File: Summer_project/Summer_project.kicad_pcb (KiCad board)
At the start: 2 copper layers, 15 parts, among them Q3 2N3904, Q4 2N3904, SW1 SW_Push

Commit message: rsc_3leds_battery
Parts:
- moved BT1 41.1 mm to (148.0, 124.0)
- moved C1 41.1 mm to (147.5, 55.0)
- moved C2 41.1 mm to (131.0, 80.5)
- moved D1 41.1 mm to (148.2, 72.0)
- moved D2 41.1 mm to (133.5, 57.0)
- moved D3 41.1 mm to (162.7, 57.0)
- moved Q3 41.1 mm to (126.5, 72.5)
- moved Q4 41.1 mm to (136.5, 72.5)
- moved R1 41.1 mm to (170.0, 93.3)
- moved R2 41.1 mm to (137.0, 85.7)
- moved R3 41.1 mm to (146.5, 85.7)
- moved R4 41.1 mm to (127.0, 85.7)
- moved R5 41.1 mm to (159.0, 85.7)
- moved SW1 41.1 mm to (151.2, 107.2)
- moved G*** 38.0 mm to (314.6, 141.0)
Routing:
- net Net-(D3-K): track 38.8 -> 40.7 mm

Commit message: _version_of_pcb_upgrades
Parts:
- moved G*** 167.0 mm to (149.0, 120.0)
- moved Q4 25.5 mm to (162.0, 72.5)
- moved C2 17.5 mm to (148.5, 79.5)
- moved C1 8.06 mm to (148.5, 63.0)
- moved Q3 7.46 mm to (134.0, 72.5)
- moved R4 6.50 mm to (133.5, 85.7)
- moved BT1 6.18 mm to (149.5, 118.0)
- moved R1 4.50 mm to (165.5, 93.3)
- moved R2 4.50 mm to (141.5, 85.7)
- moved SW1 3.81 mm to (152.8, 103.8)
- moved R3 3.00 mm to (149.5, 85.7)
- moved R5 1.50 mm to (157.5, 85.7)
- moved D1 0.27 mm to (148.0, 72.0)
- moved D3 0.27 mm to (162.5, 57.0)
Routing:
- net Net-(Q3-B): track 91.8 -> 33.5 mm
- net Net-(D2-K): track 26.2 -> 58.2 mm
- net Net-(R1-Pad1): track 54.4 -> 39.3 mm
- net Net-(D3-A): track 56.9 -> 48.6 mm
- net Net-(D3-K): track 40.7 -> 35.1 mm
- net Net-(D1-A): track 24.9 -> 20.7 mm
- net Net-(D2-A): track 49.2 -> 45.4 mm
- net Net-(BT1-+): track 19.8 -> 17.3 mm
- net Net-(Q4-B): track 36.8 -> 34.4 mm

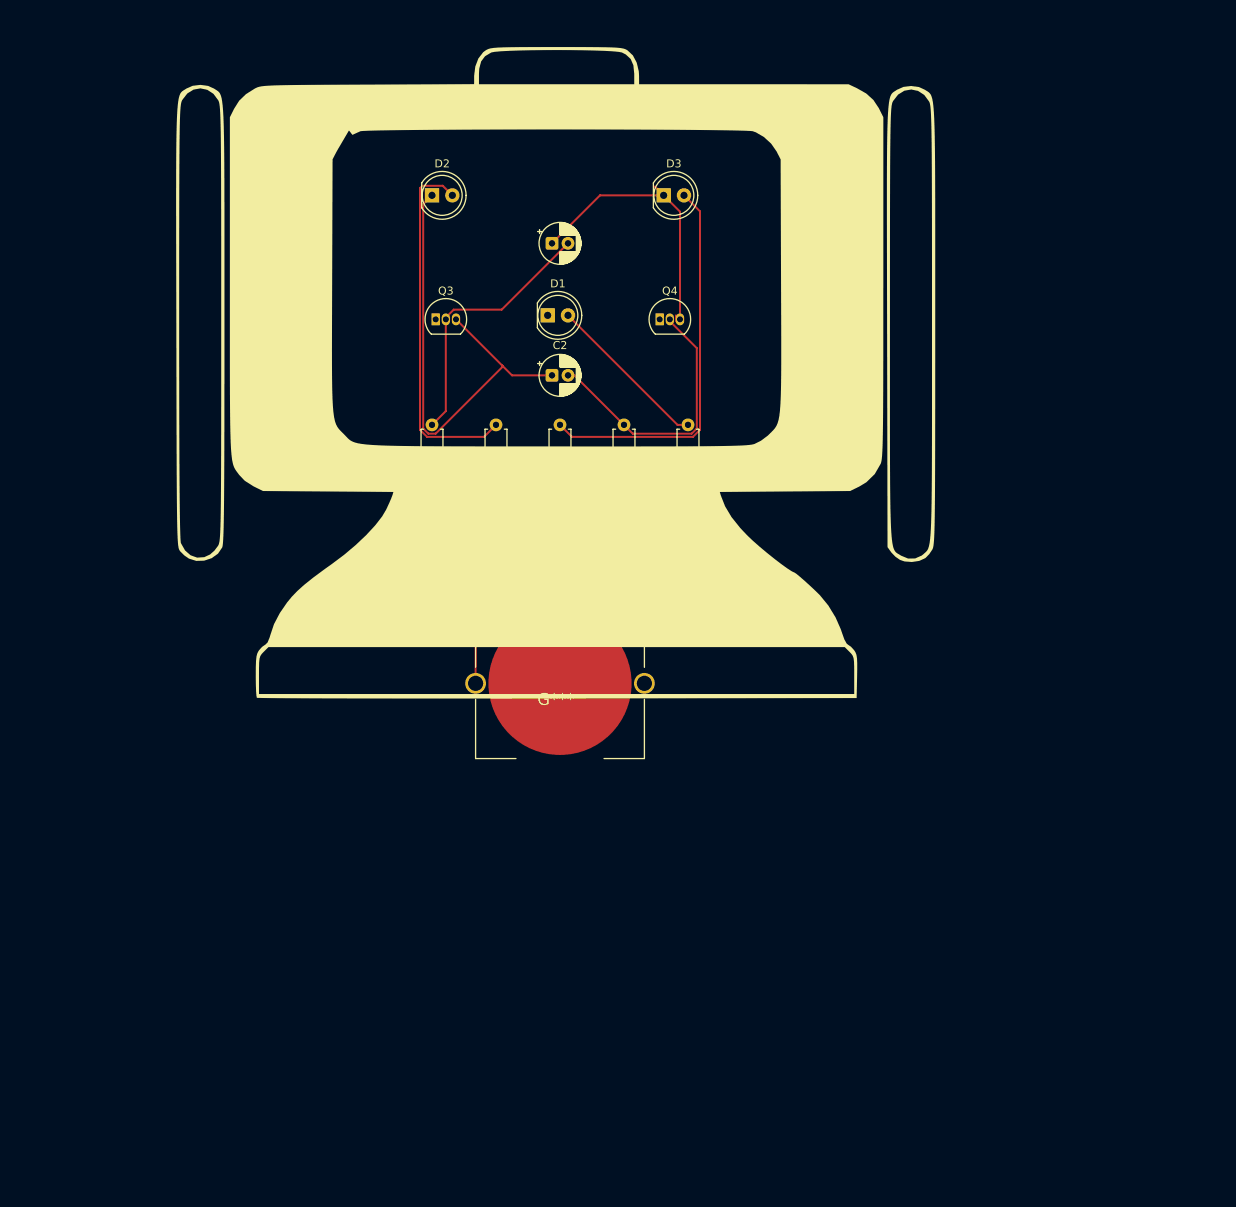
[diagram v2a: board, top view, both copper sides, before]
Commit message: edge_cut_layer_plus_capacitors_transistors_on_back_layer
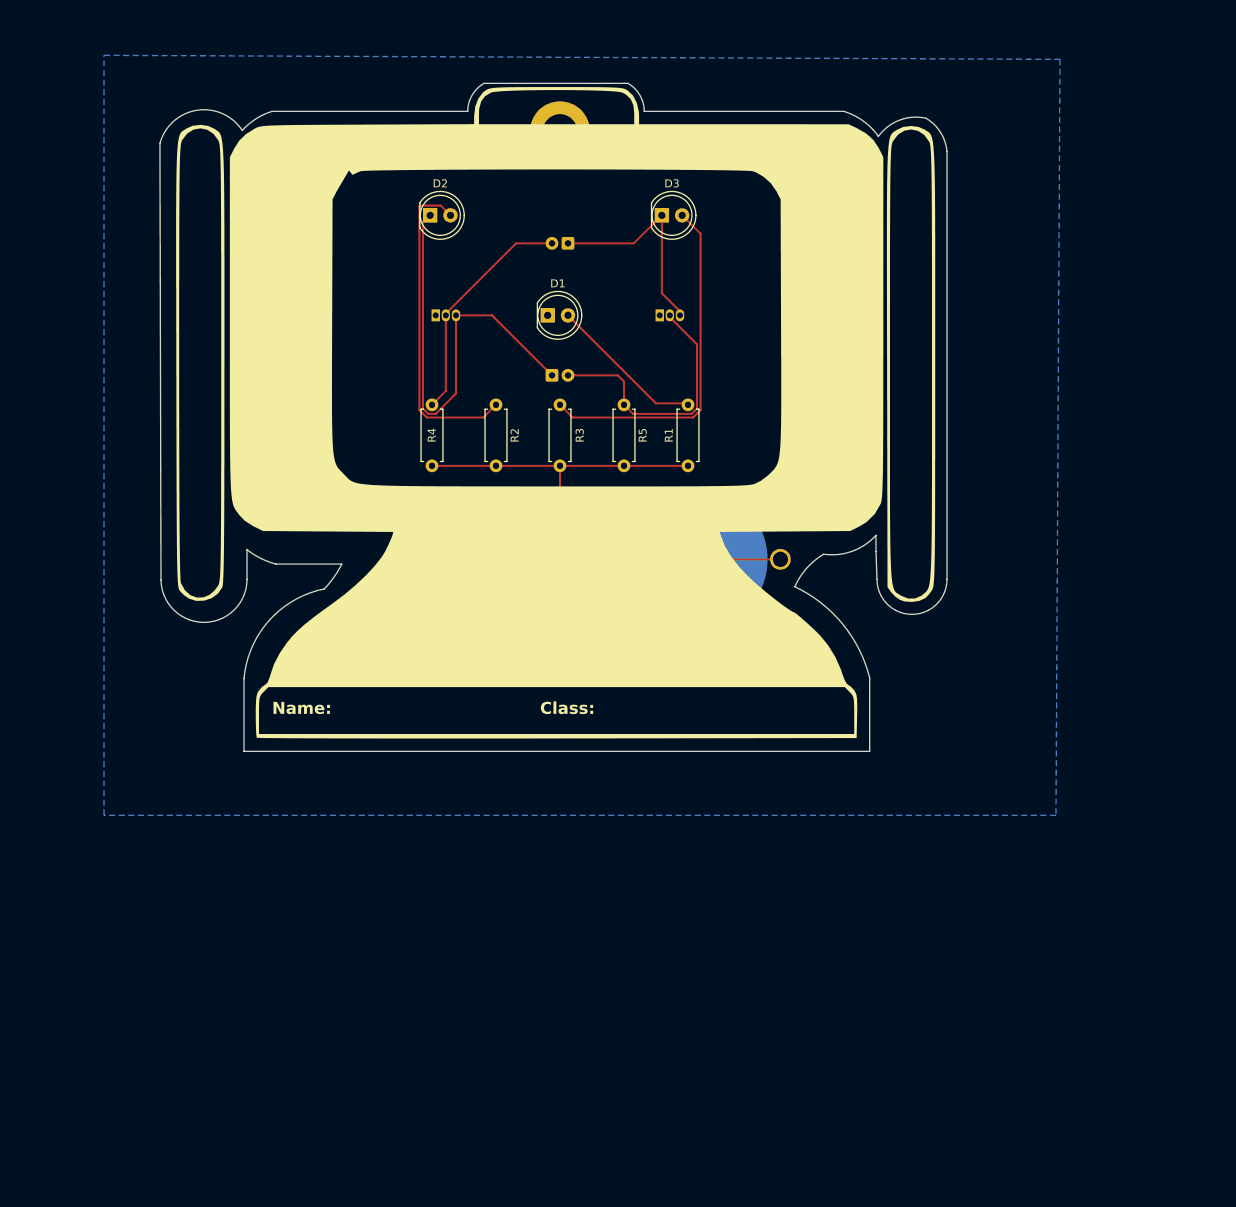
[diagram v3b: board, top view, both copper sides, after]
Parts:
- added REF**: MountingHole_4.3mm_M4_DIN965_Pad, MountingHole:MountingHole_4.3mm_M4_DIN965_Pad, F.Cu at (149.5, 49.0)
- BT1, C1, C2, Q3, Q4: moved to B.Cu
- moved BT1 23.0 mm to (166.5, 102.5), turned to 180 degrees
- moved G*** 5.00 mm to (149.0, 125.0)
- moved D3 2.51 mm to (162.2, 59.5)
- moved D2 2.51 mm to (133.3, 59.5)
- moved R1 2.50 mm to (165.5, 90.8)
- moved R2 2.50 mm to (141.5, 83.2)
- moved R3 2.50 mm to (149.5, 83.2)
- moved R4 2.50 mm to (133.5, 83.2)
- moved R5 2.50 mm to (157.5, 83.2)
- moved C1 2.00 mm to (150.5, 63.0), turned to 180 degrees
- moved Q3 0.50 mm to (134.0, 72.0)
- moved Q4 0.50 mm to (162.0, 72.0)
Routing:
- net Net-(BT1-+): track 17.3 -> 31.3 mm
- net Net-(R1-Pad1): track 39.3 -> 48.3 mm
- net Net-(D3-K): track 35.1 -> 26.6 mm
- net Net-(D2-A): track 45.4 -> 40.5 mm
- net Net-(D3-A): track 48.6 -> 43.9 mm
- net Net-(Q3-B): track 33.5 -> 30.4 mm
- net Net-(D2-K): track 58.2 -> 55.4 mm
- net Net-(Q4-B): track 34.4 -> 33.2 mm
- net Net-(D1-A): track 20.7 -> 19.7 mm
- added copper zone on B.Cu, net GND
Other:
- board outline added: 98.4 x 83.5 mm
- board text added: "Class:"
- board text added: "Name:"

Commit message: Name_without_silicon_hole_6mm
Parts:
- removed the G*** at (149.0, 125.0)
- added G***: LOGO, Summer_project:RSC_robot_with_name, F.Cu at (149.3, 133.3)
- added G***: LOGO, Summer_project:RSC_qr_code, B.Cu at (226.0, 40.9)
- moved BT1 21.4 mm to (149.5, 115.5)
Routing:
- net Net-(BT1-+): track 31.3 -> 39.4 mm
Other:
- board size 98.4 x 83.5 mm -> 97.3 x 90.7 mm
- board text added: "Designed by: Timur Kedrov"
- board text added: "RSC Summer School Badge"
- board text added: "Rev 1.0 2026"
- board text removed: "Class:"
